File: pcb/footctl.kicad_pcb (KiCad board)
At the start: 2 copper layers, 100 x 100 mm, 53 parts, among them J1 Conn_01x10_Female, J10 Conn_01x05_Female, J11 EXP2, J12 EXP1, J13 Conn_01x05_Female, J2 Conn_01x10_Female, J3 Conn_01x10_Female, J4 Conn_01x10_Female, J5 Conn_01x10_Female, J6 Conn_01x10_Female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

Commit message: fix IO mess
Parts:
- J1: value Conn_01x10_Female -> W
- J10: value Conn_01x05_Female -> PROG
- J2: value Conn_01x10_Female -> NE
- J3, J6: value Conn_01x10_Female -> SW
- J4: value Conn_01x10_Female -> NW
- J5: value Conn_01x10_Female -> E
- J7: value Conn_01x10_Female -> SE
- J8: value Conn_01x10_Female -> UPDOWN
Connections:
- net /IO0 renamed /IOLED1
- net /IO1 renamed /IOSW1
- net /IO10 renamed /IOSW5
- net /IO11 renamed /IOLED5
- net /IO12 renamed /IOSW8
- net /IO2 renamed /IOLED0
- net /IO3 renamed /IOSW0
- net /IO4 renamed /IOSW2
- net /IO5 renamed /IOLED2
- net /IO6 renamed /IOSW3
- net /IO7 renamed /IOLED3
- net /IO8 renamed /IOSW4
- net /IO9 renamed /IOLED4
- net /SOUTH1 renamed /SSW2
- net /SOUTH2 renamed /SLED2
- net /SOUTH3 renamed /SSW1
- net /SOUTH4 renamed /SLED1
- net Net-(J4-Pad1) renamed /ESW2
- net Net-(J4-Pad2) renamed /ELED2
- net Net-(J4-Pad3) renamed /ESW1
- net Net-(J4-Pad4) renamed /ELED1
- J1 pad 3: /SW1 -> Net-(J1-Pad3)
- J2 pad 3: /SW1 -> Net-(J1-Pad3)
- J2 pad 5: GND -> /SSW4
- J2 pad 6: GND -> /SLED4
- J2 pad 7: GND -> /SSW3
- J2 pad 8: GND -> /SLED3
- J3 pad 3: GND -> /SLED3
- J3 pad 4: GND -> /SSW3
- J3 pad 5: GND -> /SLED4
- J3 pad 6: GND -> /SSW4
- J6 pad 3: GND -> /IOLED7
- J6 pad 4: GND -> /IOSW7
- J6 pad 5: GND -> /IOLED6
- J6 pad 6: GND -> /IOSW6
- J8 pad 8: /IO13 -> /IOOSW9
- SW1 pad 1: /SW1 -> Net-(J1-Pad3)
- U1 pad 13: /IO13 -> /IOSW9
- U1 pad 39: Net-(U1-Pad39) -> /IOSW6
- U1 pad 40: Net-(U1-Pad40) -> /IOLED6
- U1 pad 41: Net-(U1-Pad41) -> /IOSW7
- U1 pad 45: Net-(U1-Pad45) -> /IOLED7
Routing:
- net GND: track 30.0 -> 26.9 mm, vias 23 -> 21
- net /NRST: track 22.9 -> 24.0 mm

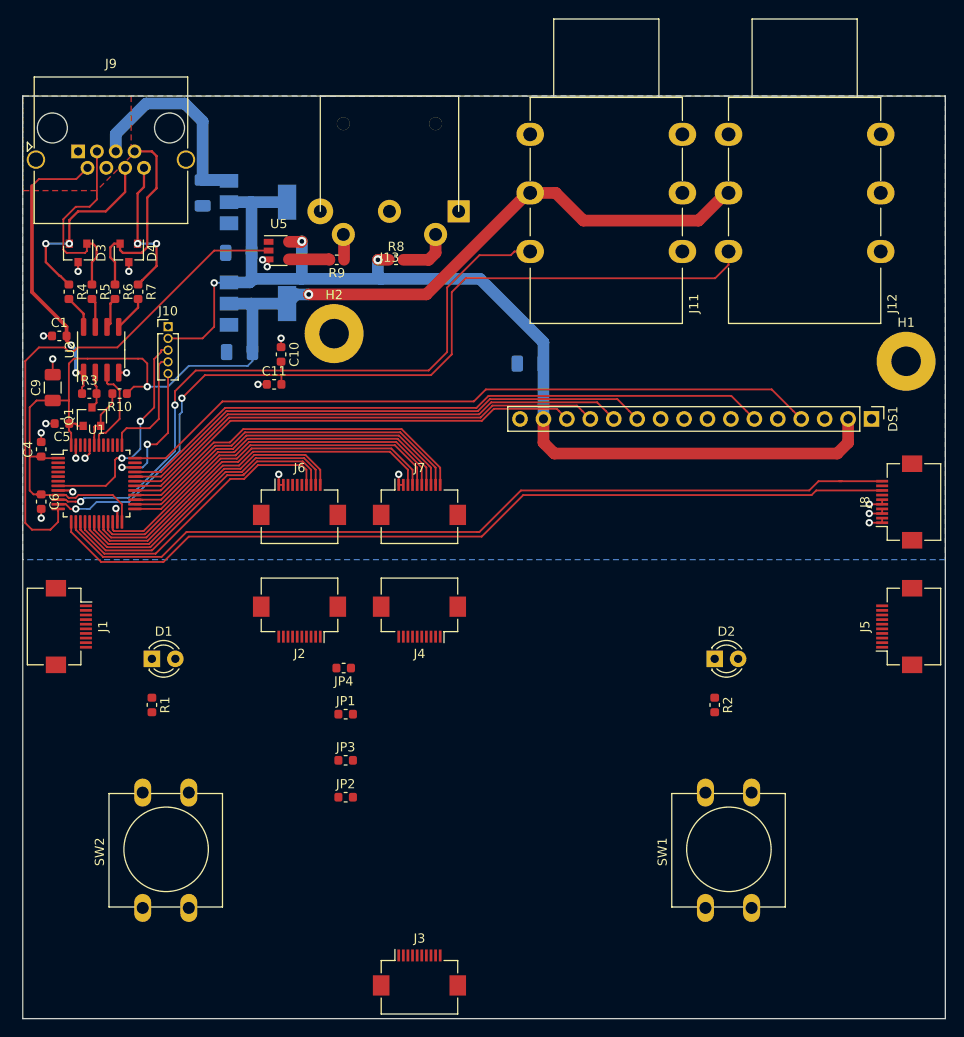
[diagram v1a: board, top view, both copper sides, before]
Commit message: mostly complete pcb, needs v-groove
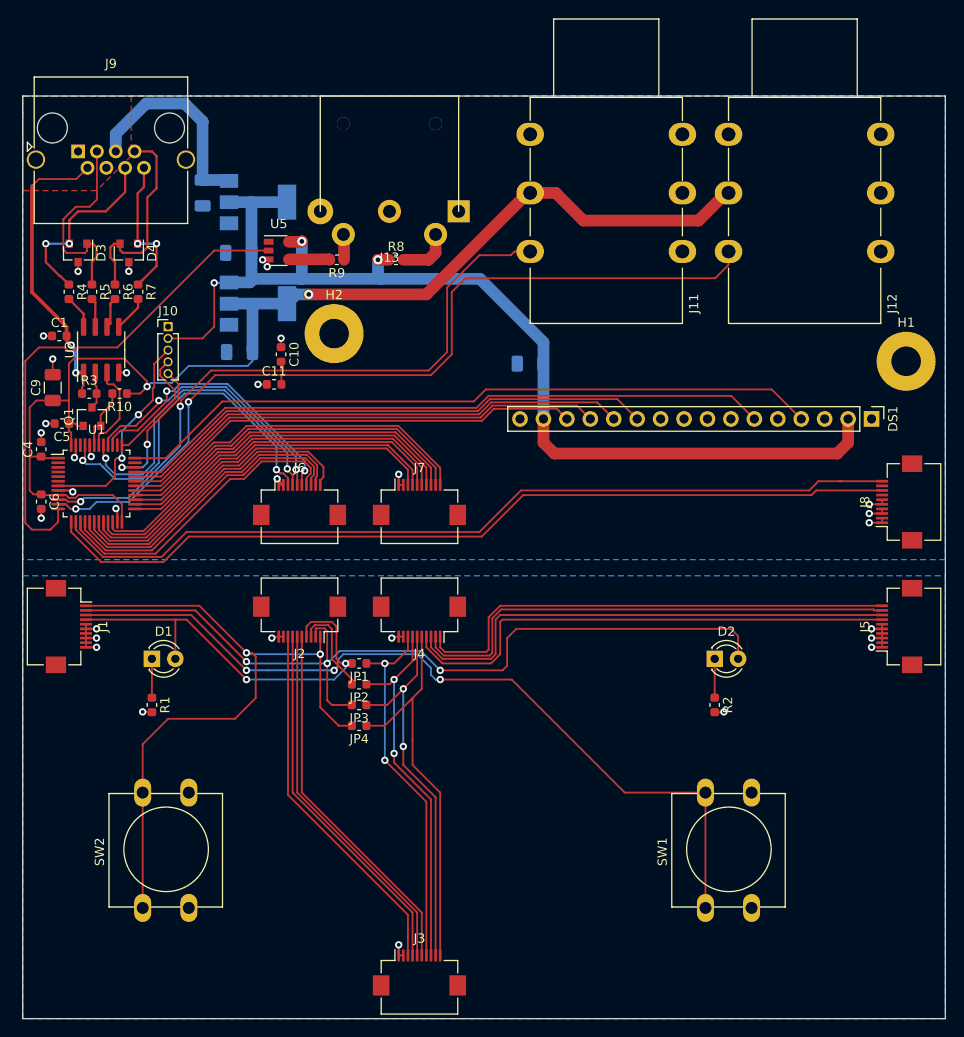
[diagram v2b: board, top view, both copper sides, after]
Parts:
- moved JP2 12.3 mm to (96.5, 93.8), turned to 180 degrees
- moved JP4 6.47 mm to (96.5, 98.2)
- moved JP3 6.18 mm to (96.5, 96.0), turned to 180 degrees
- moved JP1 5.69 mm to (96.5, 91.5), turned to 180 degrees
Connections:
- J1 pad 3: Net-(J1-Pad3) -> /SW1
- J2 pad 3: Net-(J1-Pad3) -> /SW1
- SW1 pad 1: Net-(J1-Pad3) -> /SW1
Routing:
- net /SW1: track 0.00 -> 101.3 mm, vias 0 -> 3
- net /LED2: track 0.00 -> 93.5 mm, vias 0 -> 3
- net /SW2: track 0.00 -> 77.2 mm, vias 0 -> 2
- net /ELED1: track 0.00 -> 55.3 mm
- net /ESW1: track 0.00 -> 54.7 mm
- net /ELED2: track 0.00 -> 54.2 mm
- net /ESW2: track 0.00 -> 53.4 mm
- net /LED1: track 0.00 -> 46.3 mm, vias 0 -> 2
- net /SSW2: track 0.00 -> 42.4 mm
- net /SLED2: track 0.00 -> 41.3 mm, vias 0 -> 2
- net /SSW1: track 0.00 -> 40.2 mm, vias 0 -> 2
- net /SLED1: track 0.00 -> 40.0 mm, vias 0 -> 2
- net /SSW4: track 0.00 -> 39.9 mm
- net /SSW3: track 0.00 -> 39.9 mm
- net /SLED4: track 0.00 -> 39.9 mm
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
